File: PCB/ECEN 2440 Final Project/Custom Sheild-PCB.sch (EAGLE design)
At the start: 18 parts, among them U1 V_REG_NCP50X

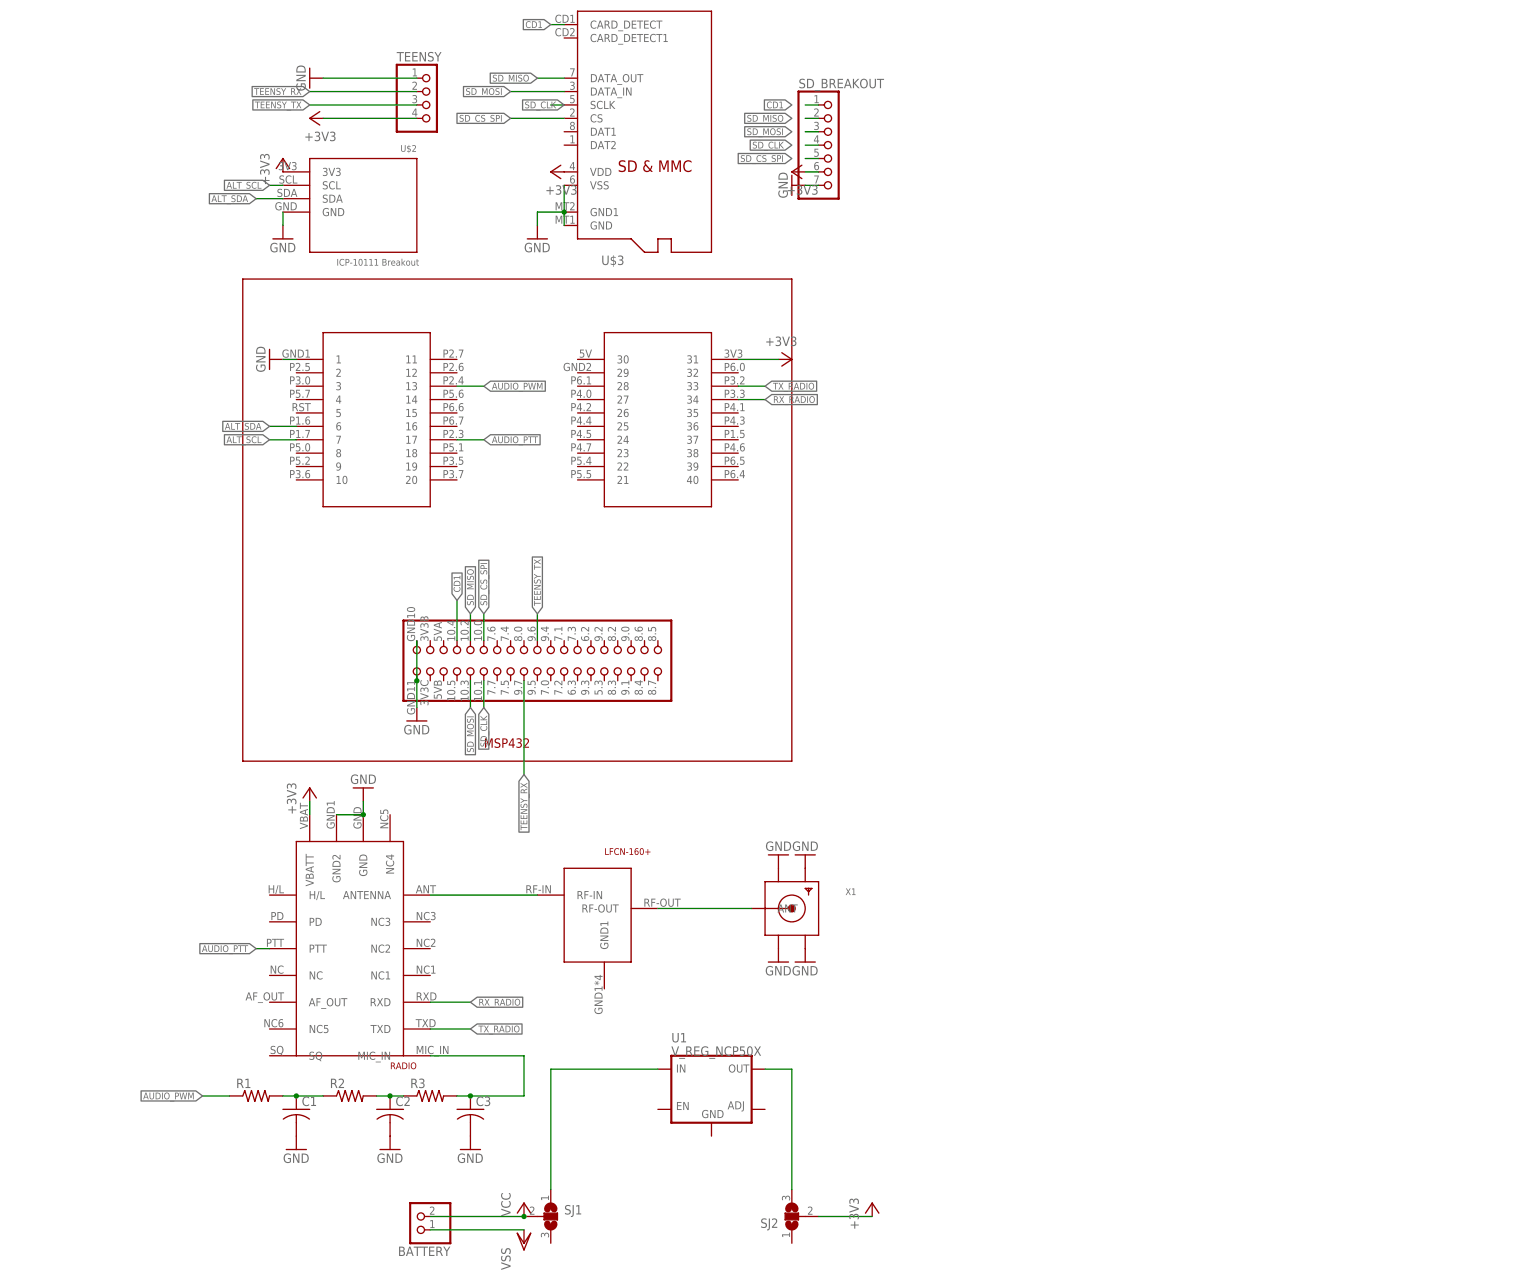
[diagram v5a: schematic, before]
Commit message: Made updates to board and created now radio breakout board
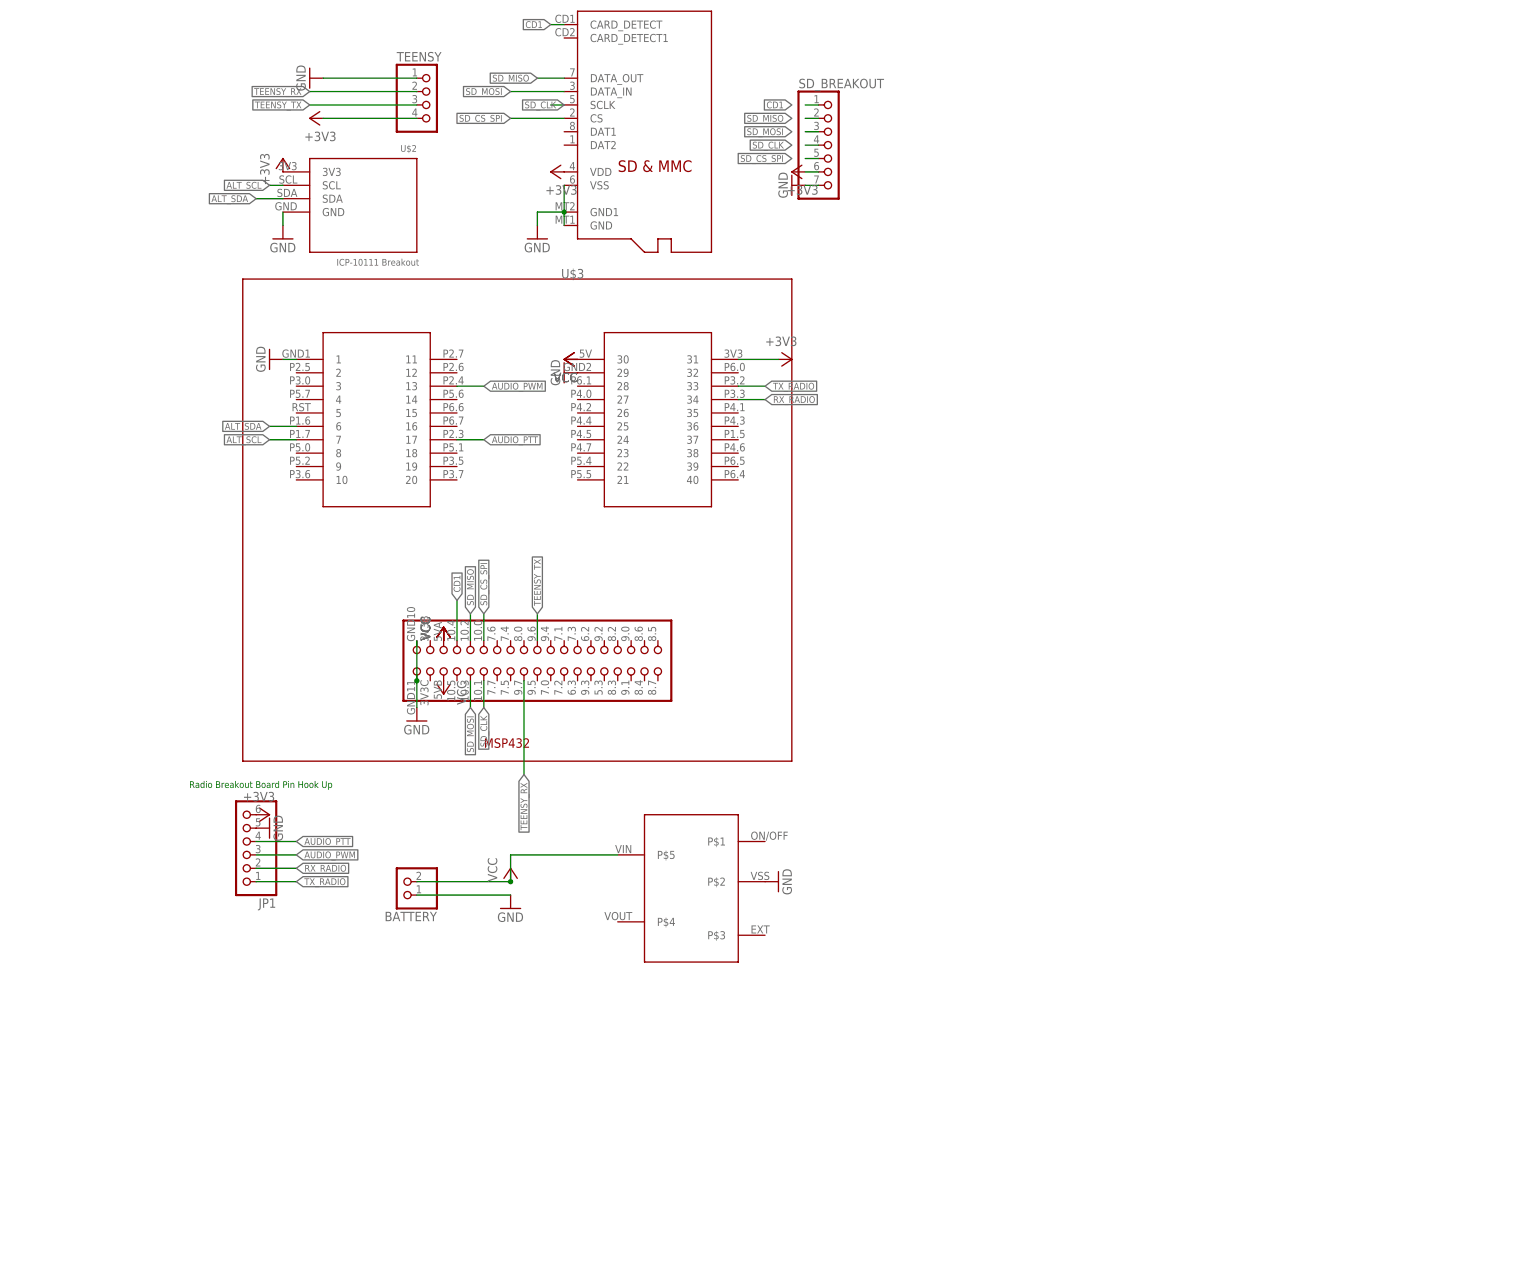
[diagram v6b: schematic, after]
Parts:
- removed C1, C2, C3: (no value), rcl:C-USC0805
- removed R1, R2, R3: (no value), rcl:R-US_R0805
- removed SJ1, SJ2: (no value), jumper:SJ2WW
- removed U$4: RADIO, Custom Library:RADIO
- removed U$6: LFCN-160+, Custom Library:LFCN-160+
- removed U1: V_REG_NCP50X, SparkFun-IC-Power:V_REG_NCP50X
- removed X1: (no value), adafruit:SMACONNECTOR_EDGE
- added JP1: (no value), pinhead:PINHD-1X6
- added U$5: LDO-S-816, Custom Library:LDO-S-816
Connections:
- removed net N$1: U$4.ANTENNA, U$6.RF-IN
- removed net N$2: C1.1, R1.2, R2.1
- removed net N$4: C2.1, R2.2, R3.1
- removed net N$5: C3.1, R3.2, U$4.MIC_IN
- removed net N$6: U$6.RF-OUT, X1.ANT
- removed net N$7: SJ1.1, U1.IN
- removed net N$8: SJ2.3, U1.OUT
- removed net VSS: BATTERY.1
- net +3V3: now also JP1.6; no longer SJ2.2, U$4.VBATT
- net AUDIO_PTT: now also JP1.4; no longer U$4.PTT
- net AUDIO_PWM: now also JP1.3; no longer R1.1
- net GND: now also BATTERY.1, JP1.5, U$3.29, U$5.P$2; no longer C1.2, C2.2, C3.2, U$4.GND, U$4.GND2, X1.GND1, X1.GND2, X1.GND3, X1.GND4
- net RX_RADIO: now also JP1.2; no longer U$4.RXD
- net TX_RADIO: now also JP1.1; no longer U$4.TXD
- net VCC: now also U$3.30, U$3.45, U$3.46, U$5.P$5; no longer SJ1.2
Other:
- note added: "Radio Breakout Board Pin Hook Up"
- moved on the sheet: BATTERY

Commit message: minor changes to board
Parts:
- removed U$5: LDO-S-816, Custom Library:LDO-S-816
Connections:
- net GND: no longer U$5.P$2
- net VCC: no longer U$5.P$5
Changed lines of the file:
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@@
 <part name="+3V7" library="supply1" library_urn="urn:adsk.eagle:library:371" deviceset="+3V3" device=""/>
 <part name="GND14" library="supply1" library_urn="urn:adsk.eagle:library:371" deviceset="GND" device=""/>
-<part name="U$5" library="Custom Library" deviceset="LDO-S-816" device=""/>
 <part name="GND15" library="supply1" library_urn="urn:adsk.eagle:library:371" deviceset="GND" device=""/>
-<part name="GND16" library="supply1" library_urn="urn:adsk.eagle:library:371" deviceset="GND" device=""/>
 <part name="P+2" library="supply1" library_urn="urn:adsk.eagle:library:371" deviceset="VCC" device=""/>
 <part name="P+3" library="supply1" library_urn="urn:adsk.eagle:library:371" deviceset="VCC" device=""/>
@@
 <attribute name="VALUE" x="93.98" y="86.36" size="1.778" layer="96" rot="R270"/>
 </instance>
-<instance part="U$5" gate="G$1" x="86.36" y="-63.5" smashed="yes" rot="R90"/>
 <instance part="GND15" gate="1" x="43.18" y="-53.34" smashed="yes">
 <attribute name="VALUE" x="40.64" y="-55.88" size="1.778" layer="96"/>
-</instance>
-<instance part="GND16" gate="1" x="93.98" y="-48.26" smashed="yes" rot="R90">
-<attribute name="VALUE" x="96.52" y="-50.8" size="1.778" layer="96" rot="R90"/>
 </instance>
 <instance part="P+2" gate="VCC" x="53.34" y="50.8" smashed="yes" rot="R90">
@@
 </segment>
 <segment>
-<pinref part="U$5" gate="G$1" pin="P$2"/>
-<pinref part="GND16" gate="1" pin="GND"/>
-</segment>
-<segment>
 <pinref part="U$3" gate="MSP432" pin="29"/>
 <pinref part="GND17" gate="1" pin="GND"/>
@@
 <wire x1="25.4" y1="-48.26" x2="43.18" y2="-48.26" width="0.1524" layer="91"/>
 <pinref part="P+1" gate="VCC" pin="VCC"/>
-<pinref part="U$5" gate="G$1" pin="P$5"/>
-<wire x1="43.18" y1="-48.26" x2="43.18" y2="-43.18" width="0.1524" layer="91"/>
-<wire x1="43.18" y1="-43.18" x2="63.5" y2="-43.18" width="0.1524" layer="91"/>
-<junction x="43.18" y="-48.26"/>
-</segment>
-<segment>
+</segment>
+<segment>

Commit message: New changes to pcb board
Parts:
- added R1, R2: 2.2k, SparkFun-Resistors:2.2KOHM-0603-1/10W-1%
- added SJ1: (no value), jumper:SJ2W
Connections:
- new net N$1: R1.2, SJ1.3
- new net N$2: R2.2, SJ1.1
- net +3V3: now also SJ1.2
- net ALT_SCL: now also R2.1
- net ALT_SDA: now also R1.1
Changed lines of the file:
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@@
 <part name="+3V4" library="supply1" library_urn="urn:adsk.eagle:library:371" deviceset="+3V3" device=""/>
 <part name="GND3" library="supply1" library_urn="urn:adsk.eagle:library:371" deviceset="GND" device=""/>
+<part name="SJ1" library="jumper" library_urn="urn:adsk.eagle:library:252" deviceset="SJ2W" device="" package3d_urn="urn:adsk.eagle:package:15474/1"/>
+<part name="R1" library="SparkFun-Resistors" library_urn="urn:adsk.eagle:library:532" deviceset="2.2KOHM" device="-0603-1/10W-1%" package3d_urn="urn:adsk.eagle:package:39650/1" value="2.2k"/>
+<part name="R2" library="SparkFun-Resistors" library_urn="urn:adsk.eagle:library:532" deviceset="2.2KOHM" device="-0603-1/10W-1%" package3d_urn="urn:adsk.eagle:package:39650/1" value="2.2k"/>
+<part name="+3V6" library="supply1" library_urn="urn:adsk.eagle:library:371" deviceset="+3V3" device=""/>
 </parts>
 <sheets>
@@
 <attribute name="VALUE" x="0" y="-40.64" size="1.778" layer="96" rot="R90"/>
 </instance>
+<instance part="SJ1" gate="G$1" x="-22.86" y="101.6" smashed="yes" rot="R270">
+<attribute name="NAME" x="-22.479" y="99.06" size="1.778" layer="95" rot="R270"/>
+<attribute name="VALUE" x="-24.765" y="99.06" size="1.778" layer="96" rot="R270"/>
+</instance>
+<instance part="R1" gate="G$1" x="-30.48" y="91.44" smashed="yes" rot="R90">
+<attribute name="NAME" x="-32.004" y="91.44" size="1.778" layer="95" font="vector" rot="R90" align="bottom-center"/>
+<attribute name="VALUE" x="-28.956" y="91.44" size="1.778" layer="96" font="vector" rot="R90" align="top-center"/>
+</instance>
+<instance part="R2" gate="G$1" x="-15.24" y="91.44" smashed="yes" rot="R90">
+<attribute name="NAME" x="-16.764" y="91.44" size="1.778" layer="95" font="vector" rot="R90" align="bottom-center"/>
+<attribute name="VALUE" x="-13.716" y="91.44" size="1.778" layer="96" font="vector" rot="R90" align="top-center"/>
+</instance>
+<instance part="+3V6" gate="G$1" x="-22.86" y="109.22" smashed="yes">
+<attribute name="VALUE" x="-25.4" y="104.14" size="1.778" layer="96" rot="R90"/>
+</instance>
 </instances>
 <busses>
@@
 <segment>
 <pinref part="U$2" gate="G$1" pin="SDA"/>
-<wire x1="-5.08" y1="81.28" x2="0" y2="81.28" width="0.1524" layer="91"/>
-<label x="-5.08" y="81.28" size="1.27" layer="95" rot="R180" xref="yes"/>
+<wire x1="-40.64" y1="81.28" x2="-30.48" y2="81.28" width="0.1524" layer="91"/>
+<label x="-40.64" y="81.28" size="1.27" layer="95" rot="R180" xref="yes"/>
+<pinref part="R1" gate="G$1" pin="1"/>
+<wire x1="-30.48" y1="81.28" x2="0" y2="81.28" width="0.1524" layer="91"/>
+<wire x1="-30.48" y1="81.28" x2="-30.48" y2="86.36" width="0.1524" layer="91"/>
+<junction x="-30.48" y="81.28"/>
 </segment>
 <segment>
@@
 <segment>
 <pinref part="U$2" gate="G$1" pin="SCL"/>
-<wire x1="-2.54" y1="83.82" x2="0" y2="83.82" width="0.1524" layer="91"/>
-<label x="-2.54" y="83.82" size="1.27" layer="95" rot="R180" xref="yes"/>
+<wire x1="-40.64" y1="83.82" x2="-15.24" y2="83.82" width="0.1524" layer="91"/>
+<label x="-40.64" y="83.82" size="1.27" layer="95" rot="R180" xref="yes"/>
+<pinref part="R2" gate="G$1" pin="1"/>
+<wire x1="-15.24" y1="83.82" x2="0" y2="83.82" width="0.1524" layer="91"/>
+<wire x1="-15.24" y1="86.36" x2="-15.24" y2="83.82" width="0.1524" layer="91"/>
+<junction x="-15.24" y="83.82"/>
 </segment>
 <segment>
@@
 <pinref part="+3V4" gate="G$1" pin="+3V3"/>
 </segment>
+<segment>
+<pinref part="SJ1" gate="G$1" pin="2"/>
+<pinref part="+3V6" gate="G$1" pin="+3V3"/>
+</segment>
 </net>
 <net name="CD1" class="0">
@@
 </segment>
 </net>
+<net name="N$1" class="0">
+<segment>
+<pinref part="R1" gate="G$1" pin="2"/>
+<wire x1="-30.48" y1="96.52" x2="-30.48" y2="101.6" width="0.1524" layer="91"/>
+<pinref part="SJ1" gate="G$1" pin="3"/>
+<wire x1="-30.48" y1="101.6" x2="-27.94" y2="101.6" width="0.1524" layer="91"/>
+</segment>
+</net>
+<net name="N$2" class="0">
+<segment>
+<pinref part="SJ1" gate="G$1" pin="1"/>
+<wire x1="-17.78" y1="101.6" x2="-15.24" y2="101.6" width="0.1524" layer="91"/>
+<pinref part="R2" gate="G$1" pin="2"/>
+<wire x1="-15.24" y1="101.6" x2="-15.24" y2="96.52" width="0.1524" layer="91"/>
+</segment>
+</net>
